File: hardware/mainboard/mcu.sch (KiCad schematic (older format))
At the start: 13 parts, among them J2 Tag-Connect SWD, J3 USB_MICRO_RIGHT, SW1 RESET, U7 ATSAMD21G18A-AUT, U8 MCP4728

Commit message: Move jackboard.pretty
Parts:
- J3: symbol MF_Connectors:USB_MICRO_RIGHT -> mainboard-rescue:USB_MICRO_RIGHT-MF_Connectors
- SW1: symbol MF_Switches:TACT_4.2MM -> mainboard-rescue:TACT_4.2MM-MF_Switches
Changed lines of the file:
@@
 RESET
 $Comp
-L MF_Switches:TACT_4.2MM SW1
+L mainboard-rescue:TACT_4.2MM-MF_Switches SW1
 U 1 1 5F0A59B0
 P 1700 7000
@@
 NoConn ~ 5700 7000
 $Comp
-L MF_Connectors:USB_MICRO_RIGHT J3
+L mainboard-rescue:USB_MICRO_RIGHT-MF_Connectors J3
 U 1 1 5F0B0468
 P 6550 5600

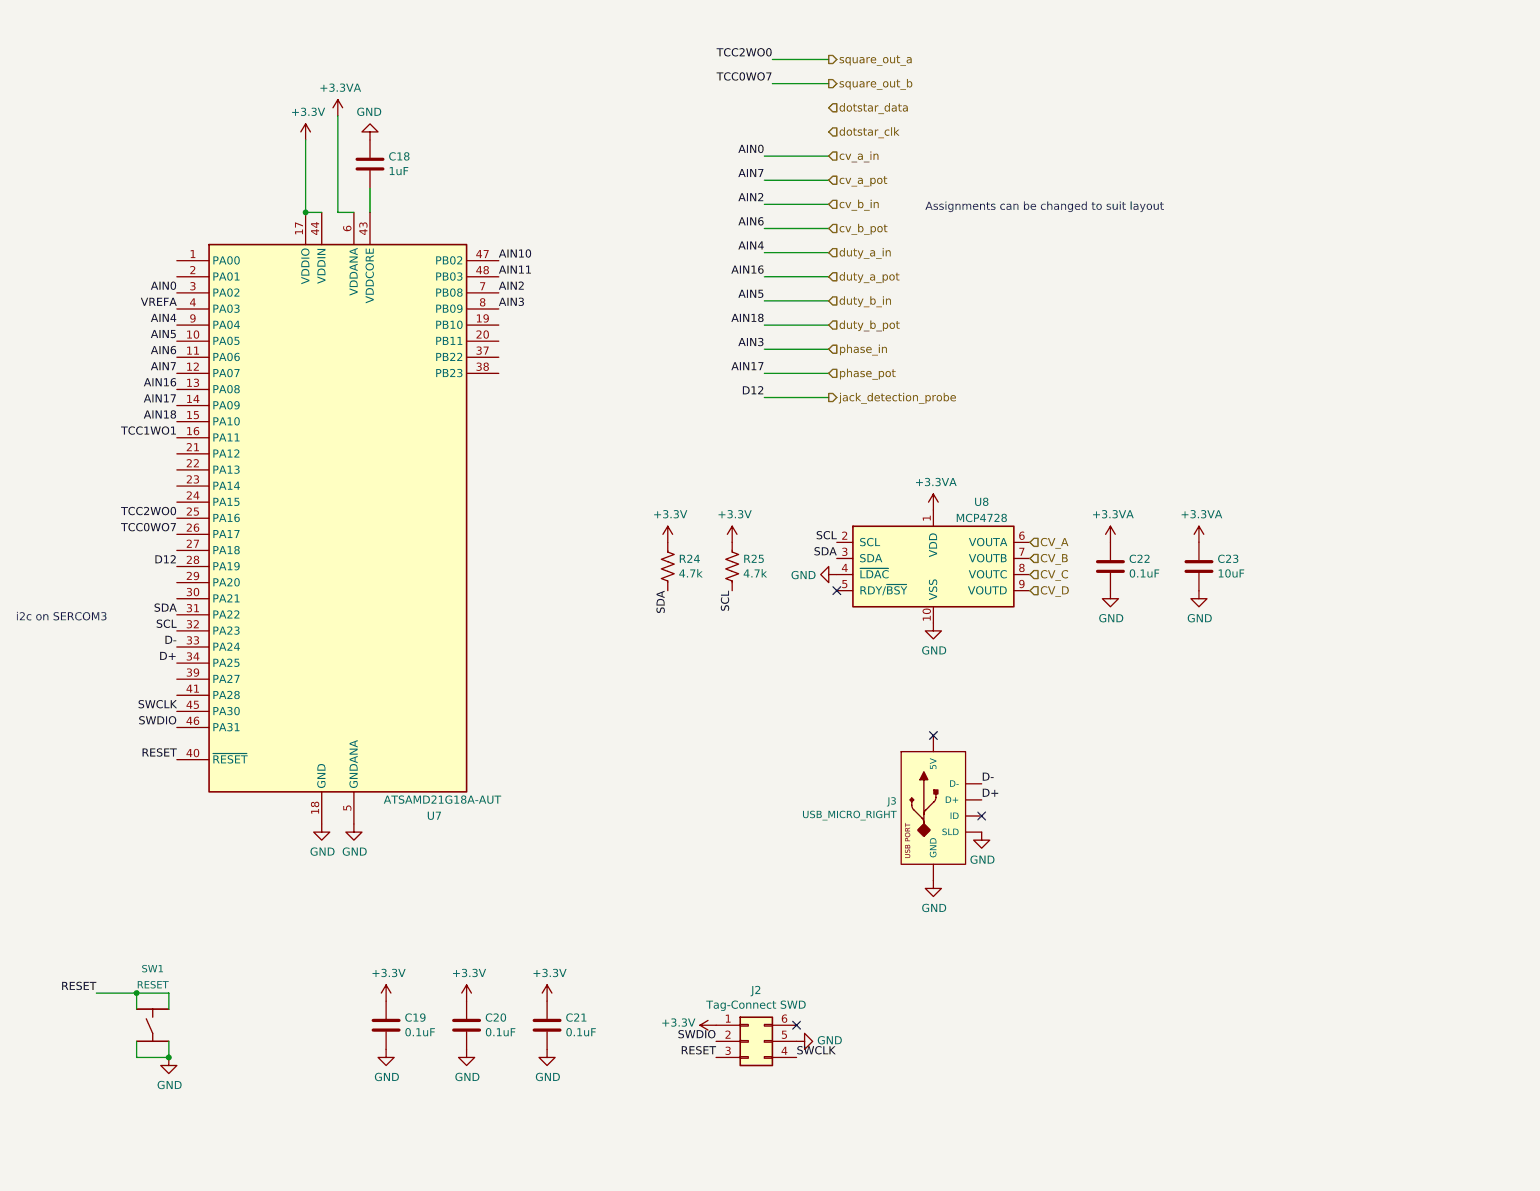
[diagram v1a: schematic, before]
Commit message: First pass layout & component selection for mainboard
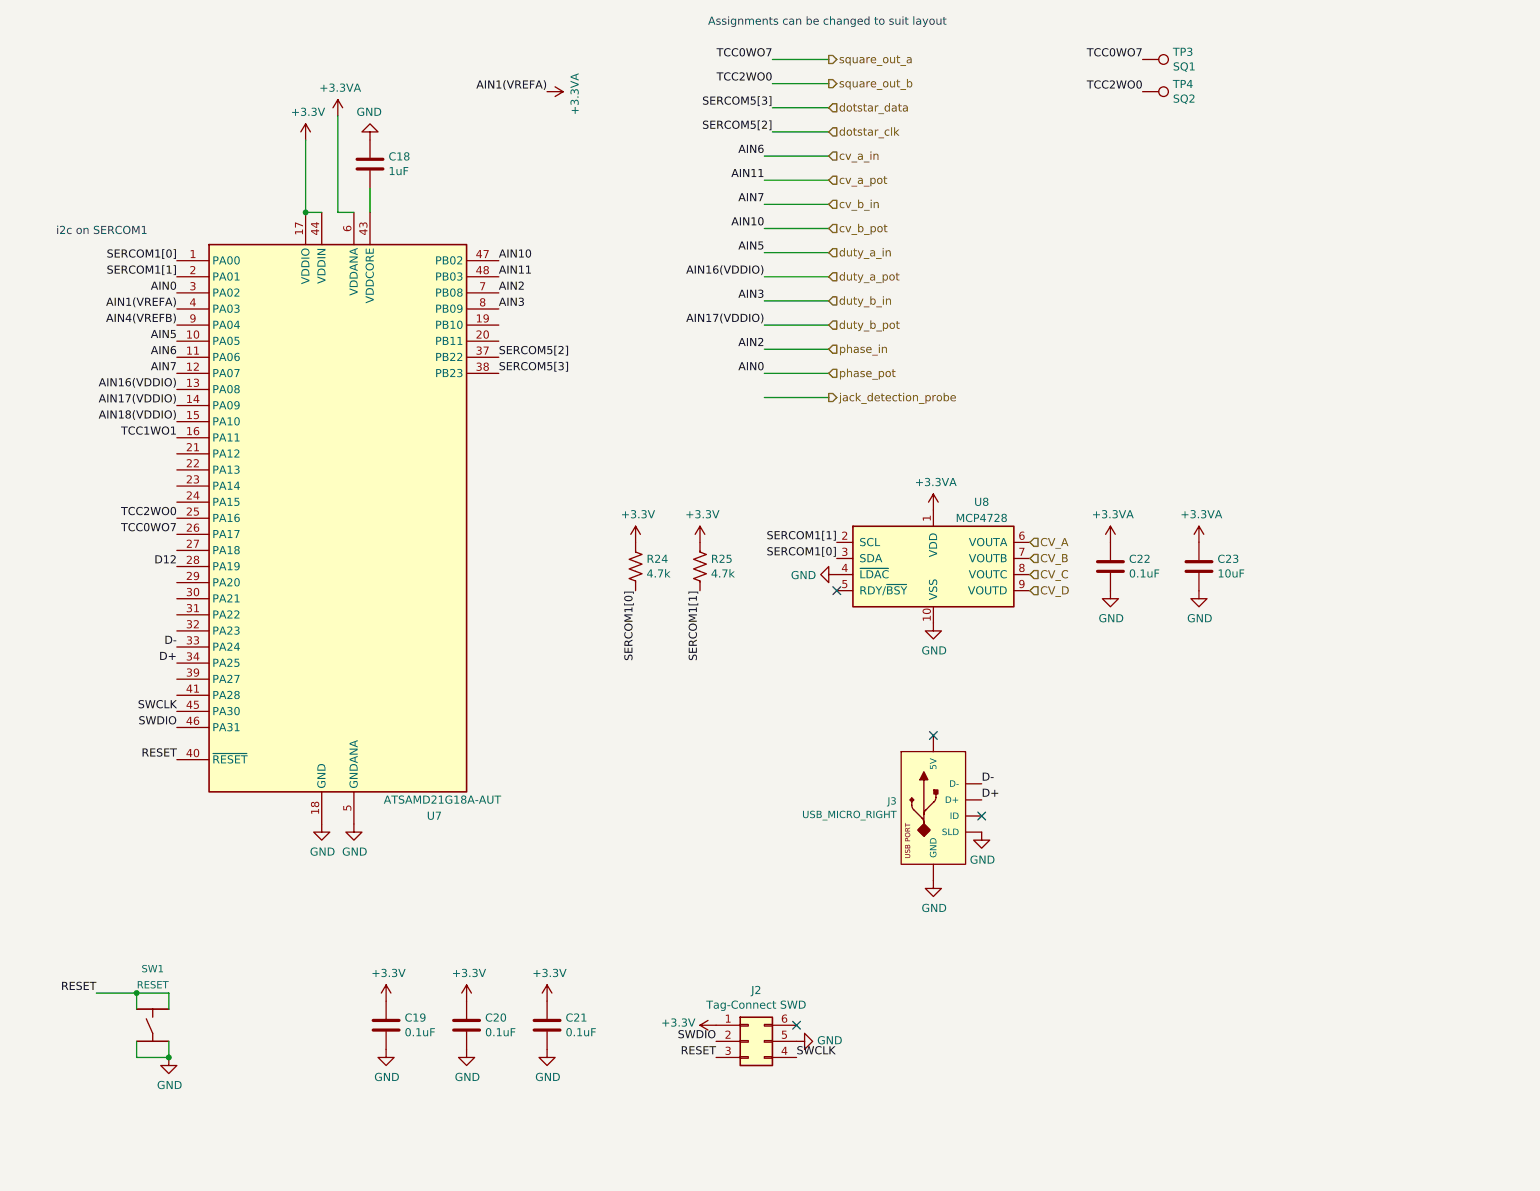
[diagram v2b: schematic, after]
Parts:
- added TP3: SQ1, TestPoint:TestPoint_Pad_D1.0mm, symbol Connector:TestPoint
- added TP4: SQ2, TestPoint:TestPoint_Pad_D1.0mm, symbol Connector:TestPoint
- C18, C19, C20, C21, C22: footprint Capacitor_SMD:C_0805_2012Metric_Pad1.15x1.40mm_HandSolder -> Capacitor_SMD:C_0603_1608Metric_Pad1.05x0.95mm_HandSolder; finalized no -> yes
- C23, J3, SW1, U7: finalized no -> yes
- J2: finalized no -> (none)
- R24, R25: footprint Resistor_SMD:R_1206_3216Metric_Pad1.42x1.75mm_HandSolder -> Resistor_SMD:R_0603_1608Metric_Pad1.05x0.95mm_HandSolder; finalized no -> yes; mpn ERA8AEB222V -> MF-RES-0603-4.7K
- U8: finalized no -> yes; mpn MCP4728 -> MCP4728A0T-E/UN
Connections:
- net labels added: AIN1(VREFA), AIN16(VDDIO), AIN17(VDDIO), AIN18(VDDIO), AIN4(VREFB), SERCOM1[0], SERCOM1[1], SERCOM5[2], SERCOM5[3]
- net labels removed: AIN16, AIN17, AIN18, AIN4, SCL, SDA, VREFA
- wire segments 25 -> 27
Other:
- note added: "i2c on SERCOM1"
- note removed: "i2c on SERCOM3"
- moved on the sheet: R24, R25

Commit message: Refine mainboard even more - ground planes, caps, oh my!
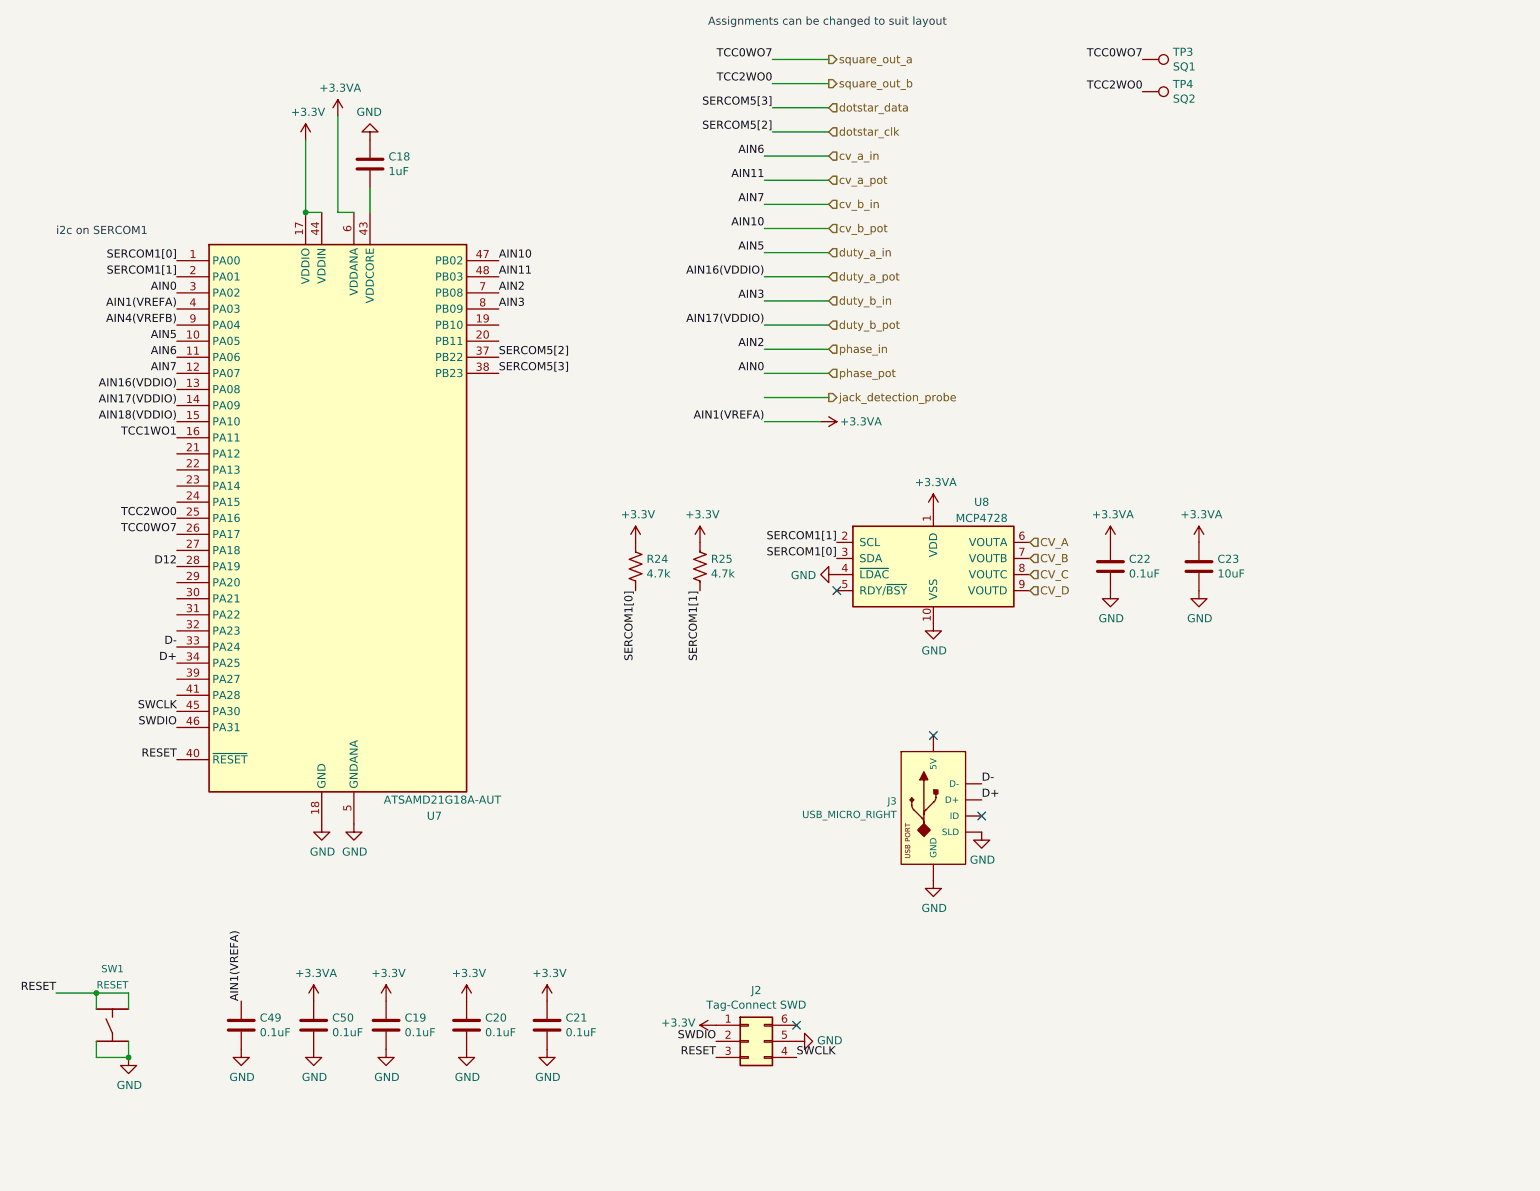
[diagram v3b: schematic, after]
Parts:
- added C49, C50: 0.1uF, Capacitor_SMD:C_0603_1608Metric_Pad1.05x0.95mm_HandSolder, symbol Device:C
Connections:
- wire segments 27 -> 28
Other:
- moved on the sheet: SW1
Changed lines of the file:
@@
 Text Label 1850 5350 2    50   ~ 0
 RESET
-Text Label 1350 6800 2    50   ~ 0
+Text Label 1100 6800 2    50   ~ 0
 RESET
 $Comp
 L mainboard-rescue:TACT_4.2MM-MF_Switches SW1
 U 1 1 5F0A59B0
-P 1700 7000
-F 0 "SW1" H 1700 7350 45  0000 C CNN
-F 1 "RESET" H 1700 7250 45  0000 C CNN
-F 2 "MF_Switches:MF_Switches-TACT4.2MM" H 1590 7150 20  0001 L CNN
-F 3 "" H 1700 7000 60  0001 C CNN
-F 4 "yes" H 1700 7000 50  0001 C CNN "finalized"
-F 5 "MF-SW-TACT-4.2MM" H 1700 7000 50  0001 C CNN "mpn"
-	1    1700 7000
-	1    0    0    -1
-$EndComp
-Wire Wire Line
-	1600 6900 1600 6800
-Wire Wire Line
-	1600 6800 1800 6800
-Wire Wire Line
-	1800 6800 1800 6900
-Wire Wire Line
-	1600 7100 1600 7200
-Wire Wire Line
-	1600 7200 1800 7200
-Wire Wire Line
-	1800 7200 1800 7100
+P 1450 7000
+F 0 "SW1" H 1450 7350 45  0000 C CNN
+F 1 "RESET" H 1450 7250 45  0000 C CNN
+F 2 "MF_Switches:MF_Switches-TACT4.2MM" H 1340 7150 20  0001 L CNN
+F 3 "" H 1450 7000 60  0001 C CNN
+F 4 "yes" H 1450 7000 50  0001 C CNN "finalized"
+F 5 "MF-SW-TACT-4.2MM" H 1450 7000 50  0001 C CNN "mpn"
+	1    1450 7000
+	1    0    0    -1
+$EndComp
+Wire Wire Line
+	1350 6900 1350 6800
+Wire Wire Line
+	1350 6800 1550 6800
+Wire Wire Line
+	1550 6800 1550 6900
+Wire Wire Line
+	1350 7100 1350 7200
+Wire Wire Line
+	1350 7200 1550 7200
+Wire Wire Line
+	1550 7200 1550 7100
 $Comp
 L power:GND #PWR047
 U 1 1 5F0A6E1E
-P 1800 7200
-F 0 "#PWR047" H 1800 6950 50  0001 C CNN
-F 1 "GND" H 1805 7027 50  0000 C CNN
-F 2 "" H 1800 7200 50  0001 C CNN
-F 3 "" H 1800 7200 50  0001 C CNN
-	1    1800 7200
-	1    0    0    -1
-$EndComp
-Connection ~ 1800 7200
-Wire Wire Line
-	1350 6800 1600 6800
-Connection ~ 1600 6800
+P 1550 7200
+F 0 "#PWR047" H 1550 6950 50  0001 C CNN
+F 1 "GND" H 1555 7027 50  0000 C CNN
+F 2 "" H 1550 7200 50  0001 C CNN
+F 3 "" H 1550 7200 50  0001 C CNN
+	1    1550 7200
+	1    0    0    -1
+$EndComp
+Connection ~ 1550 7200
+Wire Wire Line
+	1100 6800 1350 6800
+Connection ~ 1350 6800
 Text Label 1850 4650 2    50   ~ 0
 D-
@@
 Text Label 3850 2450 0    50   ~ 0
 AIN2
-Text Label 4150 1200 2    50   ~ 0
+Text Label 5500 3250 2    50   ~ 0
 AIN1(VREFA)
 Text Label 5500 2350 2    50   ~ 0
@@
 L power:+3.3VA #PWR0139
 U 1 1 5F40D255
-P 4150 1200
-F 0 "#PWR0139" H 4150 1050 50  0001 C CNN
-F 1 "+3.3VA" H 4165 1373 50  0000 C CNN
-F 2 "" H 4150 1200 50  0001 C CNN
-F 3 "" H 4150 1200 50  0001 C CNN
-	1    4150 1200
+P 5850 3250
+F 0 "#PWR0139" H 5850 3100 50  0001 C CNN
+F 1 "+3.3VA" V 5850 3500 50  0000 C CNN
+F 2 "" H 5850 3250 50  0001 C CNN
+F 3 "" H 5850 3250 50  0001 C CNN
+	1    5850 3250
 	0    1    1    0
 $EndComp
@@
 Wire Wire Line
 	5900 1300 5550 1300
+$Comp
+L Device:C C50
+U 1 1 5F2122B0
+P 2700 7000
+F 0 "C50" H 2815 7046 50  0000 L CNN
+F 1 "0.1uF" H 2815 6955 50  0000 L CNN
+F 2 "Capacitor_SMD:C_0603_1608Metric_Pad1.05x0.95mm_HandSolder" H 2738 6850 50  0001 C CNN
+F 3 "~" H 2700 7000 50  0001 C CNN
+F 4 "yes" H 2700 7000 50  0001 C CNN "finalized"
+F 5 "MF-CAP-0603-0.1uF" H 2700 7000 50  0001 C CNN "mpn"
+	1    2700 7000
+	1    0    0    -1
+$EndComp
+$Comp
+L power:+3.3VA #PWR018
+U 1 1 5F212BBB
+P 2700 6850
+F 0 "#PWR018" H 2700 6700 50  0001 C CNN
+F 1 "+3.3VA" H 2715 7023 50  0000 C CNN
+F 2 "" H 2700 6850 50  0001 C CNN
+F 3 "" H 2700 6850 50  0001 C CNN
+	1    2700 6850
+	1    0    0    -1
+$EndComp
+$Comp
+L power:GND #PWR019
+U 1 1 5F2132DD
+P 2700 7150
+F 0 "#PWR019" H 2700 6900 50  0001 C CNN
+F 1 "GND" H 2705 6977 50  0000 C CNN
+F 2 "" H 2700 7150 50  0001 C CNN
+F 3 "" H 2700 7150 50  0001 C CNN
+	1    2700 7150
+	1    0    0    -1
+$EndComp
+$Comp
+L Device:C C49
+U 1 1 5F215056
+P 2250 7000
+F 0 "C49" H 2365 7046 50  0000 L CNN
+F 1 "0.1uF" H 2365 6955 50  0000 L CNN
+F 2 "Capacitor_SMD:C_0603_1608Metric_Pad1.05x0.95mm_HandSolder" H 2288 6850 50  0001 C CNN
+F 3 "~" H 2250 7000 50  0001 C CNN
+F 4 "yes" H 2250 7000 50  0001 C CNN "finalized"
+F 5 "MF-CAP-0603-0.1uF" H 2250 7000 50  0001 C CNN "mpn"
+	1    2250 7000
+	1    0    0    -1
+$EndComp
+$Comp
+L power:GND #PWR015
+U 1 1 5F21506A
+P 2250 7150
+F 0 "#PWR015" H 2250 6900 50  0001 C CNN
+F 1 "GND" H 2255 6977 50  0000 C CNN
+F 2 "" H 2250 7150 50  0001 C CNN
+F 3 "" H 2250 7150 50  0001 C CNN
+	1    2250 7150
+	1    0    0    -1
+$EndComp
+Text Label 2250 6850 1    50   ~ 0
+AIN1(VREFA)
+Wire Wire Line
+	5500 3250 5850 3250
 $EndSCHEMATC

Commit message: Fixup ERC errors
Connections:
- no-connect marks 4 -> 22
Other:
- moved on the sheet: C22, C23, J3, R24, R25, U8
